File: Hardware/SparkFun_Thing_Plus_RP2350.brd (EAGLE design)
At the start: 22.9 x 58.4 mm, 149 parts, among them J1 THING_PLUS_LOGICAL, J3 QWIIC_RIGHT_ANGLE, J6 MICRO-SDFRICTION, Q1 100mA/20V/3.8Ω, U1 RP2350A, U2 RM2, U3 RT9080-33GJ5, U4 LM66200, U5 W25QXX128MBIT, U6 MCP73831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

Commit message: Update Eagle libs
Add PROD_ID for RM2
Update Eagle libs for updated version of RT9080 and LM66200
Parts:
- U4: device SparkFun_Thing_Plus_RA6M5:SOT8 -> SparkFun-IC-Power:SOT8
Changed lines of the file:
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@@
 <element name="U2" library="RM2" package="RM2" value="RM2" x="11.43" y="50.165" smashed="yes">
 <attribute name="NAME" x="11.43" y="59.165" size="0.6096" layer="25" font="vector" ratio="20" align="center"/>
+<attribute name="PROD_ID" value="IC-21607" x="11.43" y="50.165" size="1.778" layer="27" display="off"/>
 <attribute name="VALUE" x="11.43" y="40.665" size="0.6096" layer="27" font="vector" ratio="20" align="center"/>
 </element>
@@
 <attribute name="VALUE" x="8.763" y="16.518" size="0.6096" layer="28" font="vector" ratio="20" rot="MR90" align="top-center"/>
 </element>
-<element name="U4" library="SparkFun_Thing_Plus_RA6M5" package="SOT8" value="LM66200" x="6.985" y="16.51" smashed="yes" rot="MR0">
+<element name="U4" library="SparkFun-IC-Power" package="SOT8" value="LM66200" x="6.985" y="16.51" smashed="yes" rot="MR0">
 <attribute name="PROD_ID" value="IC-20783" x="6.985" y="16.51" size="1.778" layer="28" font="vector" ratio="15" rot="MR0" display="off"/>
 </element>

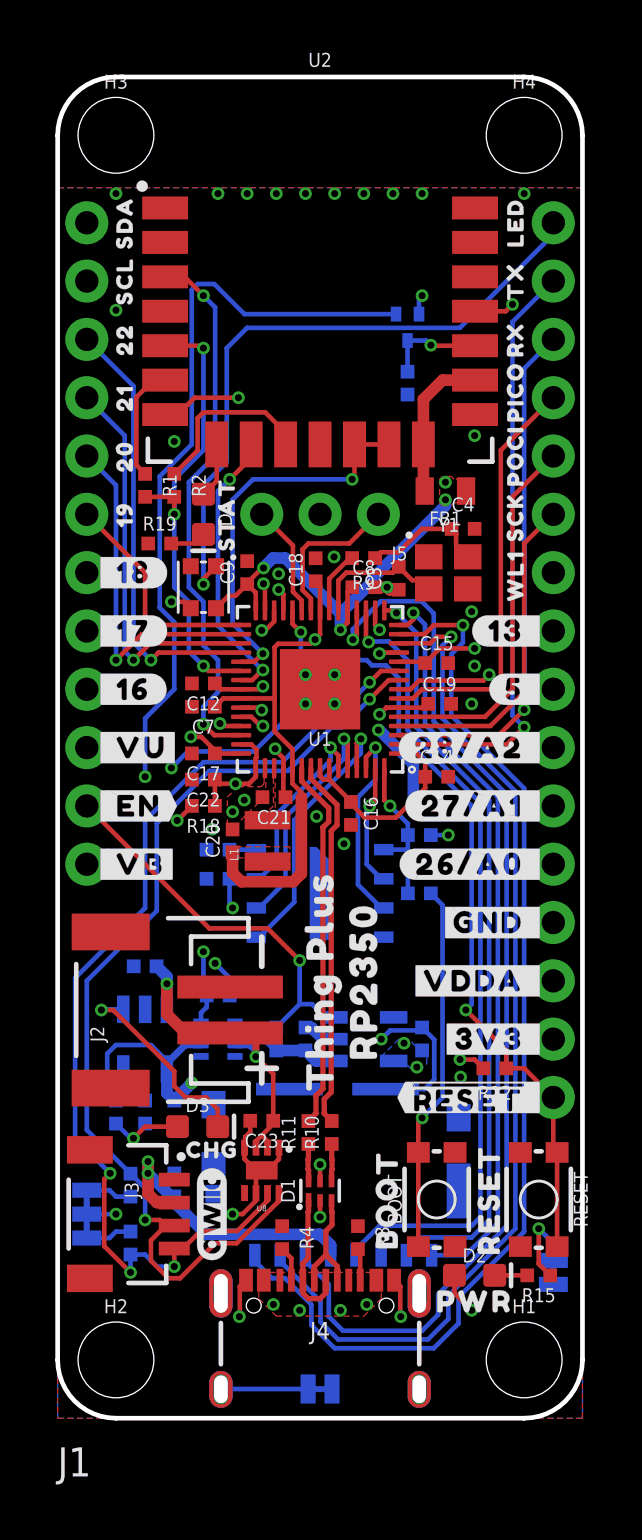
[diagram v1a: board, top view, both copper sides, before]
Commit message: Remove SD card SDIO
SDIO can only be achieved via the PIO, and support for it is questionable. Changing to SPI frees up 5 GPIO that can be used for other purposes.
Change SD card socket to CONN-20948
Connect SPI pins to SD card socket
Connect SD card detection pin to GPIO pin
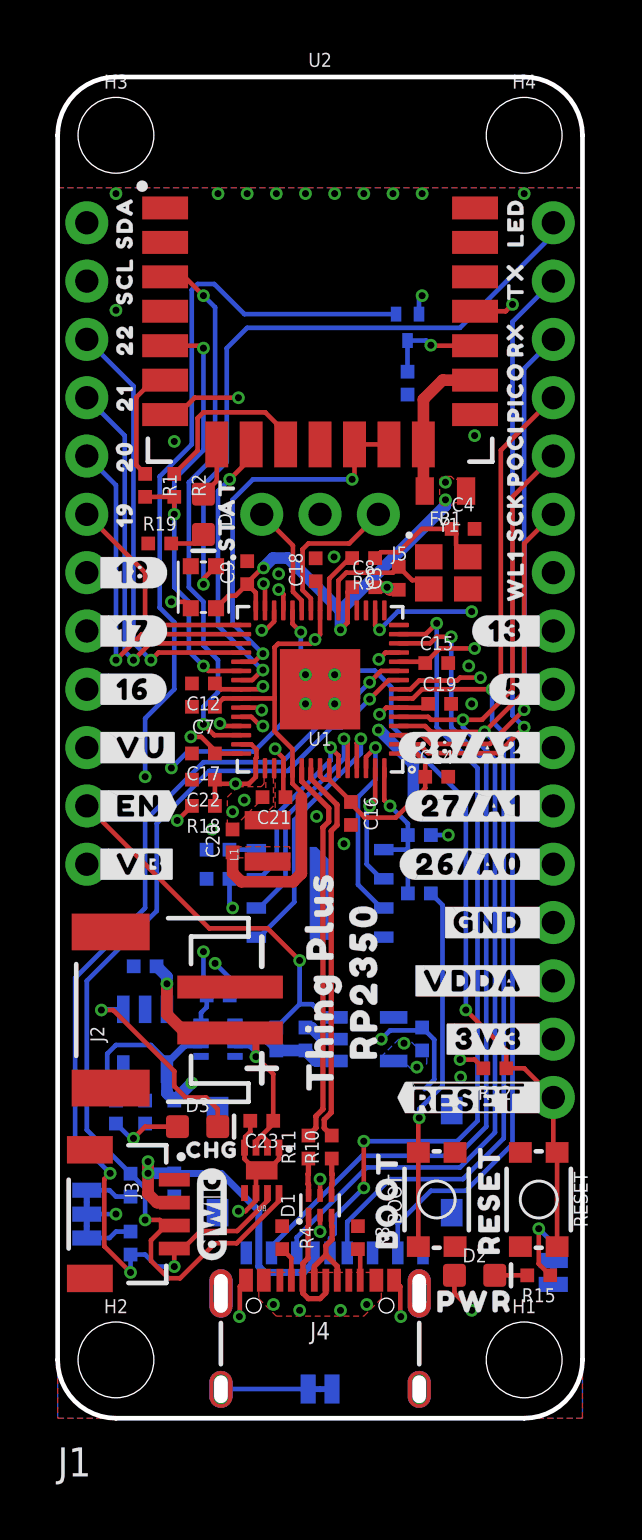
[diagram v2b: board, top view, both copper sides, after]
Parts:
- J6: value MICRO-SDFRICTION -> MICRO-SD-ATOM; device SparkFun-Connectors:MICROSD_TINY -> SparkFun-Connectors:MICROSD_ATOM
- moved D1 0.63 mm to (11.4, 9.27)
- moved R10 0.63 mm to (11.9, 11.8)
- moved R11 0.63 mm to (10.9, 11.8)
- moved J6 0.24 mm to (12.1, 11.2)
- turned C24 to 270 degrees
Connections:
- net SD_!CS!/D3 renamed SD_!CS!
- removed net SD_D1: J6.8, U1.15
- removed net SD_D2: J6.1, U1.14
- removed net SD_PICO/CMD: J6.3, U1.19
- removed net SD_POCI/D0: J6.7, U1.16
- removed net SD_SCLK: J6.5, U1.18
- new net !SD_DET!: J6.9, U1.14
- net GND: now also J6.SHIELD1, J6.SHIELD2, J6.SHIELD3, J6.SHIELD4; no longer J6.GND1, J6.GND2, J6.GND3, J6.GND4, J6.GND5, J6.GND6
- net PICO: now also J6.3
- net POCI: now also J6.7
- net SCK: now also J6.5
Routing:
- net SD_D2: track 47.7 -> 0.00 mm, vias 1 -> 0
- net SD_PICO/CMD: track 47.5 -> 0.00 mm, vias 1 -> 0
- net SD_SCLK: track 35.3 -> 0.00 mm, vias 1 -> 0
- net !SD_DET!: track 0.00 -> 35.0 mm, vias 0 -> 3
- net SD_POCI/D0: track 33.1 -> 0.00 mm, vias 1 -> 0
- net SD_D1: track 32.6 -> 0.00 mm, vias 1 -> 0
- net PICO: track 16.3 -> 46.2 mm, vias 0 -> 1
- net SCK: track 14.3 -> 42.3 mm, vias 0 -> 1
- net POCI: track 18.0 -> 45.9 mm, vias 0 -> 1
- net SD_!CS!: track 44.7 -> 36.2 mm
- net GND: track 31.7 -> 29.7 mm
- net 3.3V: track 67.2 -> 68.3 mm
- net USB_D_N: track 16.2 -> 16.9 mm
- net N$8: track 5.10 -> 4.47 mm
- net N$7: track 5.91 -> 5.28 mm
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
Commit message: Fix SD card detection being active high
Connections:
- net !SD_DET! renamed SD_DET
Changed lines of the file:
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@@
 <wire x1="19.513" y1="48.215" x2="19.812" y2="48.514" width="0.2032" layer="1"/>
 </signal>
-<signal name="!SD_DET!">
+<signal name="SD_DET">
 <contactref element="J6" pad="9"/>
 <wire x1="12.065" y1="8.763" x2="12.065" y2="8.036" width="0.2032" layer="16"/>

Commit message: Add peripheral power control
Add a second voltage regulator dedicated to powering the WS2812, uSD card, and Qwiic connector
Change pinout of A4 and A5 of Thing Plus pinout to make routing easier, and replace RM2 GPIO with RP2350 GPIO
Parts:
- removed U$71: (no value), output:#_WL1#0
- added C13: 2.2uF, SparkFun-Capacitors:0402-TIGHT
- added C25: 0.1uF, SparkFun-Capacitors:0402-TIGHT
- added LP: JUMPER-SMT_2_NC_TRACE_SILK, SparkFun-Jumpers:SMT-JUMPER_2_NC_TRACE_SILK
- added R21: 10k, SparkFun-Resistors:0402-TIGHT
- added R22: 1M, SparkFun-Resistors:0402-TIGHT
- added U$72: (no value), output:#VA_#0
- added U$73: (no value), output:#_VA#0
- added U9: RT9080-33GJ5, SparkFun-IC-Power:SOT23-5
- U$18: device output:#_VDDA#0 -> output:##RST#_#0
- U$26: device output:#VDDA_#0 -> output:#LP#0
- U$28: device output:##RESET#_#0 -> output:#11_#0
- U$65: device output:#13_#0 -> output:#12_#0
- U$66: device output:WL10 -> output:#_12#0
- U$70: device output:#_13#0 -> output:#_11#0
- moved U$28 20.3 mm to (21.3, 34.3)
- moved C24 12.7 mm to (15.9, 16.9), flipped to the top, turned to 90 degrees
- moved U$26 8.89 mm to (12.4, 19.1), flipped to the bottom
- moved U$18 5.08 mm to (21.3, 14.0), flipped to the top
- moved U$44 2.54 mm to (11.4, 21.6)
- moved U$45 2.54 mm to (13.3, 21.6)
- moved U$65 2.54 mm to (21.3, 36.8)
- moved U$66 1.40 mm to (21.3, 36.8), flipped to the bottom, turned to 0 degrees
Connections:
- removed net GPIO13: J1.20, U1.17
- removed net WL_GPIO1: J1.19, U2.C4
- new net 3.3V_SW: C24.1, C25.1, I2C.2, J3.2, J6.4, U7.VCC, U9.5
- new net GPIO11: J1.20, U1.15
- new net GPIO12: J1.19, U1.16
- new net PERIPH_POW: R21.1, R22.2, U1.17, U9.3
- new net VIN: C1.1, C13.1, R7.1, U3.1, U4.2, U4.7, U9.1
- net 3.3V: now also LP.2; no longer C24.1, I2C.2, J3.2, J6.4, U7.VCC
- net GND: now also C13.2, C25.2, R22.1, U9.2
- net N$11: now also LP.1, R21.2; no longer C1.1, R7.1, U3.1, U4.2, U4.7
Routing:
- net 3.3V_SW: track 0.00 -> 59.5 mm, vias 0 -> 7
- net PERIPH_POW: track 0.00 -> 29.2 mm, vias 0 -> 2
- net 3.3V: track 68.3 -> 50.5 mm, vias 22 -> 20
- net WL_GPIO1: track 15.1 -> 0.00 mm, vias 1 -> 0
- net GPIO13: track 9.17 -> 0.00 mm, vias 2 -> 0
- net VIN: track 0.00 -> 9.03 mm, vias 0 -> 1
- net GPIO12: track 0.00 -> 8.36 mm, vias 0 -> 1
- net GPIO11: track 0.00 -> 6.89 mm, vias 0 -> 1
- net N$11: track 6.29 -> 2.23 mm, vias 0 -> 1
- net WL_D: track 20.4 -> 22.0 mm
- net SD_DET: track 35.0 -> 34.0 mm
- net GPIO19: track 9.84 -> 10.9 mm
- net GPIO20: track 15.3 -> 16.1 mm
- net !BOOT!: track 16.0 -> 16.7 mm
- net GPIO22: track 19.2 -> 19.9 mm
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
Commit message: Connect fuel gauge alert pin
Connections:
- new net !BATT_ALERT!: U1.19, U8.5
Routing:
- net !BATT_ALERT!: track 0.00 -> 38.8 mm, vias 0 -> 3
- net SD_DET: track 34.0 -> 34.8 mm
- net SCK: track 42.3 -> 42.9 mm
- net POCI: track 45.9 -> 46.5 mm
- net SD_!CS!: track 35.7 -> 36.3 mm
- net PICO: track 46.2 -> 46.8 mm
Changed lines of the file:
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@@
 <wire x1="14.815" y1="7.201" x2="14.815" y2="8.465" width="0.2032" layer="16"/>
 <wire x1="14.815" y1="8.465" x2="16.256" y2="9.906" width="0.2032" layer="16"/>
-<wire x1="16.256" y1="9.906" x2="17.78" y2="9.906" width="0.2032" layer="16"/>
-<wire x1="17.78" y1="9.906" x2="19.812" y2="11.938" width="0.2032" layer="16"/>
-<wire x1="19.812" y1="11.938" x2="19.812" y2="29.464" width="0.2032" layer="16"/>
-<wire x1="19.812" y1="29.464" x2="18.923" y2="30.353" width="0.2032" layer="16"/>
+<wire x1="16.256" y1="9.906" x2="18.288" y2="9.906" width="0.2032" layer="16"/>
+<wire x1="18.288" y1="9.906" x2="20.193" y2="11.811" width="0.2032" layer="16"/>
+<wire x1="20.193" y1="11.811" x2="20.193" y2="29.083" width="0.2032" layer="16"/>
+<wire x1="20.193" y1="29.083" x2="18.923" y2="30.353" width="0.2032" layer="16"/>
 <wire x1="18.923" y1="30.353" x2="18.923" y2="31.75" width="0.2032" layer="16"/>
 <via x="18.923" y="31.75" extent="1-16" drill="0.3048"/>
@@
 <contactref element="J6" pad="3"/>
 <wire x1="10.415" y1="7.201" x2="10.415" y2="7.875" width="0.2032" layer="16"/>
-<wire x1="10.415" y1="7.875" x2="13.462" y2="10.922" width="0.2032" layer="16"/>
-<wire x1="13.462" y1="10.922" x2="17.526" y2="10.922" width="0.2032" layer="16"/>
-<wire x1="17.526" y1="10.922" x2="19.05" y2="12.446" width="0.2032" layer="16"/>
-<wire x1="19.05" y1="12.446" x2="19.05" y2="28.702" width="0.2032" layer="16"/>
-<wire x1="19.05" y1="28.702" x2="17.653" y2="30.099" width="0.2032" layer="16"/>
+<wire x1="10.415" y1="7.875" x2="13.208" y2="10.668" width="0.2032" layer="16"/>
+<wire x1="13.208" y1="10.668" x2="17.78" y2="10.668" width="0.2032" layer="16"/>
+<wire x1="17.78" y1="10.668" x2="19.431" y2="12.319" width="0.2032" layer="16"/>
+<wire x1="19.431" y1="12.319" x2="19.431" y2="28.321" width="0.2032" layer="16"/>
+<wire x1="19.431" y1="28.321" x2="17.653" y2="30.099" width="0.2032" layer="16"/>
 <wire x1="17.653" y1="30.099" x2="17.653" y2="30.423" width="0.2032" layer="16"/>
 <via x="17.653" y="30.423" extent="1-16" drill="0.3048"/>
@@
 <contactref element="J6" pad="5"/>
 <wire x1="12.615" y1="7.201" x2="12.615" y2="8.551" width="0.2032" layer="16"/>
-<wire x1="12.615" y1="8.551" x2="14.478" y2="10.414" width="0.2032" layer="16"/>
-<wire x1="14.478" y1="10.414" x2="17.653" y2="10.414" width="0.2032" layer="16"/>
-<wire x1="17.653" y1="10.414" x2="19.431" y2="12.192" width="0.2032" layer="16"/>
-<wire x1="19.431" y1="29.058" x2="18.593" y2="29.896" width="0.2032" layer="16"/>
+<wire x1="12.615" y1="8.551" x2="14.351" y2="10.287" width="0.2032" layer="16"/>
+<wire x1="14.351" y1="10.287" x2="18.034" y2="10.287" width="0.2032" layer="16"/>
+<wire x1="18.034" y1="10.287" x2="19.812" y2="12.065" width="0.2032" layer="16"/>
+<wire x1="19.812" y1="28.677" x2="18.593" y2="29.896" width="0.2032" layer="16"/>
 <via x="18.593" y="29.896" extent="1-16" drill="0.3048"/>
-<wire x1="19.431" y1="12.192" x2="19.431" y2="29.058" width="0.2032" layer="16"/>
+<wire x1="19.812" y1="12.065" x2="19.812" y2="28.677" width="0.2032" layer="16"/>
 </signal>
 <signal name="GPIO26/A0">
@@
 <wire x1="16.034" y1="33.75" x2="14.8665" y2="33.75" width="0.2032" layer="1"/>
 <via x="17.018" y="33.655" extent="1-16" drill="0.3048"/>
-<wire x1="18.669" y1="12.7" x2="18.669" y2="28.575" width="0.2032" layer="16"/>
-<wire x1="18.669" y1="28.575" x2="17.018" y2="30.226" width="0.2032" layer="16"/>
+<wire x1="19.05" y1="12.573" x2="19.05" y2="28.194" width="0.2032" layer="16"/>
+<wire x1="19.05" y1="28.194" x2="17.018" y2="30.226" width="0.2032" layer="16"/>
 <wire x1="17.018" y1="33.655" x2="17.018" y2="30.226" width="0.2032" layer="16"/>
 <contactref element="J6" pad="2"/>
 <wire x1="9.315" y1="7.201" x2="9.315" y2="7.4832" width="0.2032" layer="16"/>
-<wire x1="9.315" y1="7.4832" x2="13.2618" y2="11.43" width="0.2032" layer="16"/>
-<wire x1="13.2618" y1="11.43" x2="17.399" y2="11.43" width="0.2032" layer="16"/>
-<wire x1="17.399" y1="11.43" x2="18.669" y2="12.7" width="0.2032" layer="16"/>
+<wire x1="9.315" y1="7.4832" x2="12.8808" y2="11.049" width="0.2032" layer="16"/>
+<wire x1="12.8808" y1="11.049" x2="17.526" y2="11.049" width="0.2032" layer="16"/>
+<wire x1="17.526" y1="11.049" x2="19.05" y2="12.573" width="0.2032" layer="16"/>
 </signal>
 <signal name="LED_IN">
@@
 <wire x1="12.065" y1="8.763" x2="13.335" y2="10.033" width="0.2032" layer="16"/>
 <via x="13.335" y="10.033" extent="1-16" drill="0.3048"/>
-<wire x1="13.97" y1="12.065" x2="13.97" y2="10.668" width="0.2032" layer="1"/>
-<wire x1="13.335" y1="10.033" x2="13.97" y2="10.668" width="0.2032" layer="1"/>
-<via x="13.97" y="12.065" extent="1-16" drill="0.3048"/>
-<wire x1="13.97" y1="12.065" x2="17.399" y2="12.065" width="0.2032" layer="16"/>
-<wire x1="17.399" y1="12.065" x2="18.288" y2="12.954" width="0.2032" layer="16"/>
-<wire x1="18.288" y1="12.954" x2="18.288" y2="28.321" width="0.2032" layer="16"/>
-<wire x1="18.288" y1="28.321" x2="16.51" y2="30.099" width="0.2032" layer="16"/>
+<wire x1="13.335" y1="11.557" x2="13.335" y2="10.033" width="0.2032" layer="1"/>
+<via x="13.335" y="11.557" extent="1-16" drill="0.3048"/>
+<wire x1="13.335" y1="11.557" x2="13.462" y2="11.43" width="0.2032" layer="16"/>
+<wire x1="17.272" y1="11.43" x2="13.462" y2="11.43" width="0.2032" layer="16"/>
+<wire x1="17.272" y1="11.43" x2="18.669" y2="12.827" width="0.2032" layer="16"/>
+<wire x1="18.669" y1="12.827" x2="18.669" y2="27.94" width="0.2032" layer="16"/>
+<wire x1="18.669" y1="27.94" x2="16.51" y2="30.099" width="0.2032" layer="16"/>
 <contactref element="U1" pad="14"/>
 <via x="16.51" y="34.11686875" extent="1-16" drill="0.3048"/>
@@
 <via x="17.78" y="20.574" extent="1-16" drill="0.3048"/>
 <wire x1="17.78" y1="20.574" x2="17.907" y2="20.701" width="0.2032" layer="16"/>
-<wire x1="17.907" y1="20.701" x2="17.907" y2="27.813" width="0.2032" layer="16"/>
-<wire x1="17.907" y1="27.813" x2="15.24" y2="30.48" width="0.2032" layer="16"/>
+<wire x1="17.907" y1="20.701" x2="17.907" y2="27.432" width="0.2032" layer="16"/>
+<wire x1="17.907" y1="27.432" x2="15.24" y2="30.099" width="0.2032" layer="16"/>
 <wire x1="15.24" y1="33.02" x2="13.97" y2="34.29" width="0.2032" layer="16"/>
 <via x="13.97" y="34.29" extent="1-16" drill="0.3048"/>
-<wire x1="15.24" y1="30.48" x2="15.24" y2="33.02" width="0.2032" layer="16"/>
+<wire x1="15.24" y1="30.099" x2="15.24" y2="33.02" width="0.2032" layer="16"/>
 <contactref element="U1" pad="17"/>
 <wire x1="13.83" y1="35.1865" x2="13.83" y2="34.43" width="0.2032" layer="1"/>
@@
 <wire x1="17.3915" y1="35.1865" x2="14.23" y2="35.1865" width="0.2032" layer="1"/>
 </signal>
+<signal name="!BATT_ALERT!">
+<contactref element="U8" pad="5"/>
+<contactref element="U1" pad="19"/>
+<wire x1="13.03" y1="35.1865" x2="13.03" y2="34.341" width="0.2032" layer="1"/>
+<wire x1="13.03" y1="34.341" x2="13.081" y2="34.29" width="0.2032" layer="1"/>
+<via x="13.081" y="34.29" extent="1-16" drill="0.3048"/>
+<wire x1="13.081" y1="34.29" x2="13.589" y2="34.798" width="0.2032" layer="16"/>
+<wire x1="13.589" y1="34.798" x2="14.732" y2="34.798" width="0.2032" layer="16"/>
+<wire x1="14.732" y1="34.798" x2="15.875" y2="33.655" width="0.2032" layer="16"/>
+<wire x1="15.875" y1="33.655" x2="15.875" y2="30.099" width="0.2032" layer="16"/>
+<wire x1="15.875" y1="30.099" x2="18.288" y2="27.686" width="0.2032" layer="16"/>
+<wire x1="18.288" y1="27.686" x2="18.288" y2="13.081" width="0.2032" layer="16"/>
+<wire x1="18.288" y1="13.081" x2="17.018" y2="11.811" width="0.2032" layer="16"/>
+<wire x1="13.843" y1="11.811" x2="13.589" y2="12.065" width="0.2032" layer="16"/>
+<wire x1="17.018" y1="11.811" x2="13.843" y2="11.811" width="0.2032" layer="16"/>
+<wire x1="13.589" y1="12.065" x2="12.065" y2="12.065" width="0.2032" layer="16"/>
+<wire x1="10.414" y1="10.414" x2="10.287" y2="10.414" width="0.2032" layer="16"/>
+<via x="10.287" y="10.414" extent="1-16" drill="0.3048"/>
+<wire x1="12.065" y1="12.065" x2="10.414" y2="10.414" width="0.2032" layer="16"/>
+<wire x1="10.287" y1="10.414" x2="7.747" y2="10.414" width="0.2032" layer="15"/>
+<wire x1="7.747" y1="10.414" x2="7.62" y2="10.287" width="0.2032" layer="15"/>
+<via x="7.62" y="10.287" extent="1-16" drill="0.3048"/>
+<wire x1="7.62" y1="10.287" x2="7.785" y2="10.287" width="0.2032" layer="1"/>
+<wire x1="8.14" y1="9.932" x2="8.14" y2="9.805" width="0.2032" layer="1"/>
+<wire x1="8.14" y1="9.932" x2="7.785" y2="10.287" width="0.2032" layer="1"/>
+</signal>
 </signals>

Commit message: Design review updates
Change version number to v02 (significant changes made since v01)
Add version number to copper
Add voltage regulator voltage and current specifications to schematic
Fix swapped POCI and PICO silk
Add test point for BOOT button
Fix acid traps
Add GND vias for each decoupling cap of U1
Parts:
- added TP1: TEST-POINT3X5, SparkFun-Connectors:PAD.03X.05
- moved U$5 2.79 mm to (19.9, 41.9)
- moved U$6 2.79 mm to (19.9, 44.7)
- moved U$4 0.25 mm to (19.9, 47.2)
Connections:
- net !BOOT!: now also TP1.1
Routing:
- net GND: track 29.6 -> 30.4 mm, vias 35 -> 40
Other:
- board text added: "v02"

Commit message: Design review updates
Reposition fuel gauge and charge LED to get more clearance around them
Reposition power LED and resistor for better clearance
Add fiducials
Add measures
Fix TX and RX Buzzard tails
Fix acid trap
Improve GND pours
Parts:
- added FD1, FD2, FD3, FD4: FIDUCIALUFIDUCIAL, SparkFun-Aesthetics:FIDUCIAL-MICRO
- moved FRAME1 63.7 mm to (52.1, -8.89)
- moved LOGO3 4.19 mm to (4.51, 5.33), turned to 0 degrees
- moved U8 2.29 mm to (7.62, 8.89)
- moved C23 1.98 mm to (7.62, 11.4)
- moved U$49 1.94 mm to (5.08, 12.7)
- moved D3 1.52 mm to (7.62, 12.7)
- moved D2 0.13 mm to (18.2, 6.10)
- moved R15 0.13 mm to (21.0, 6.10)
- moved U$62 0.13 mm to (18.2, 4.95)
- turned PWR to 270 degrees
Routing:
- net V_BATT: track 26.8 -> 29.5 mm
- net !BATT_ALERT!: track 38.8 -> 41.2 mm
- net SCL: track 72.0 -> 69.8 mm
- net GND: track 30.4 -> 32.5 mm, vias 40 -> 43
- net N$19: track 3.89 -> 1.82 mm
- net SDA: track 73.2 -> 71.1 mm
- net N$21: track 3.16 -> 4.68 mm
- net N$22: track 8.97 -> 10.0 mm
- net 3.3V_SW: track 59.8 -> 58.8 mm
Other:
- board text added: "Dryw Wade"
